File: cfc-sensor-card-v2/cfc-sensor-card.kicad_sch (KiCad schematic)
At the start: 6 parts

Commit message: Schematic Changes
Made schematic into hierarchy view. Revised OPD to match modern OPD. Removed connectors page. Separated power sequencing and PIRT sensor into 2 pages.
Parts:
- added J1: TFM-120-01-L-D-RA, oresat-connectors:J-SAMTEC-TFM-120-X1-XXX-D-RA, symbol oresat-connectors:J-SAMTEC-TFM-120-01-L-D-RA
- added J2: J-SAMTEC-TFM-110-X1-XXX-D-RA, oresat-connectors:J-SAMTEC-TFM-110-X1-XXX-D-RA, symbol oresat-connectors:J-SAMTEC-TFM-110-01-L-D-RA
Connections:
- new net C3-UART-RX: J1.38
- new net C3-UART-TX: J1.37
- new net CAN1_H: J1.33, J1.34
- new net CAN1_L: J1.35, J1.36
- new net CAN2_H: J1.17, J1.18
- new net CAN2_L: J1.19, J1.20
- new net GND: J1.27, J1.28, J1.29, J1.30
- new net OPD/OPD_PWR: J1.15, J1.16
- new net OPD/OPD_SCL: J1.13, J1.14
- new net OPD/OPD_SDA: J1.11, J1.12
- new net OUT1_N: J2.5, J2.6
- new net OUT1_P: J2.7, J2.8
- new net SENSOR_ENABLE: J2.13, J2.14
- new net SPI_CLK: J2.17, J2.18
- new net SPI_MISO: J2.15, J2.16
- new net SPI_MOSI: J2.19, J2.20
- new net TEC_ENABLE: J2.10, J2.9
- new net THERM+: J2.11, J2.12
- new net TXCLK_N: J2.1, J2.2
- new net TXCLK_P: J2.3, J2.4
- new net VBUS: J1.23, J1.24, J1.25, J1.26
- new net ~{SD}: J1.39, J1.40
- no-connect marks 0 -> 21
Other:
- sheet PIRT Sensor renamed Power Seqeuncing
- removed sheet Connectors
- added sheet PIRT (cfc-sensor-card-sch-PIRT.kicad_sch)
- sheet OPD ports: added OPD_PWR, OPD_SCL, OPD_SDA; removed none
- sheet Power Seqeuncing: file cfc-sensor-card-sch-pirt.kicad_sch -> cfc-sensor-card-sch-power.kicad_sch
- sheet Power Seqeuncing ports: added CLK_EN, SENSOR_ENABLE; removed none
- sheet TEC Control ports: added TEC+, TEC-, TEC_ENABLE; removed none
- note added: "Aux Connector"
- note added: "Future: route a "power is on" signal to the CFC Processor Card so it knows directly if the CFC Sensor Card is powered up or not."
- note added: "Main OreSat Card Connector (Backplane v2)"
- moved on the sheet: FID1, FID2, FID3, FID4, FID5, FID6

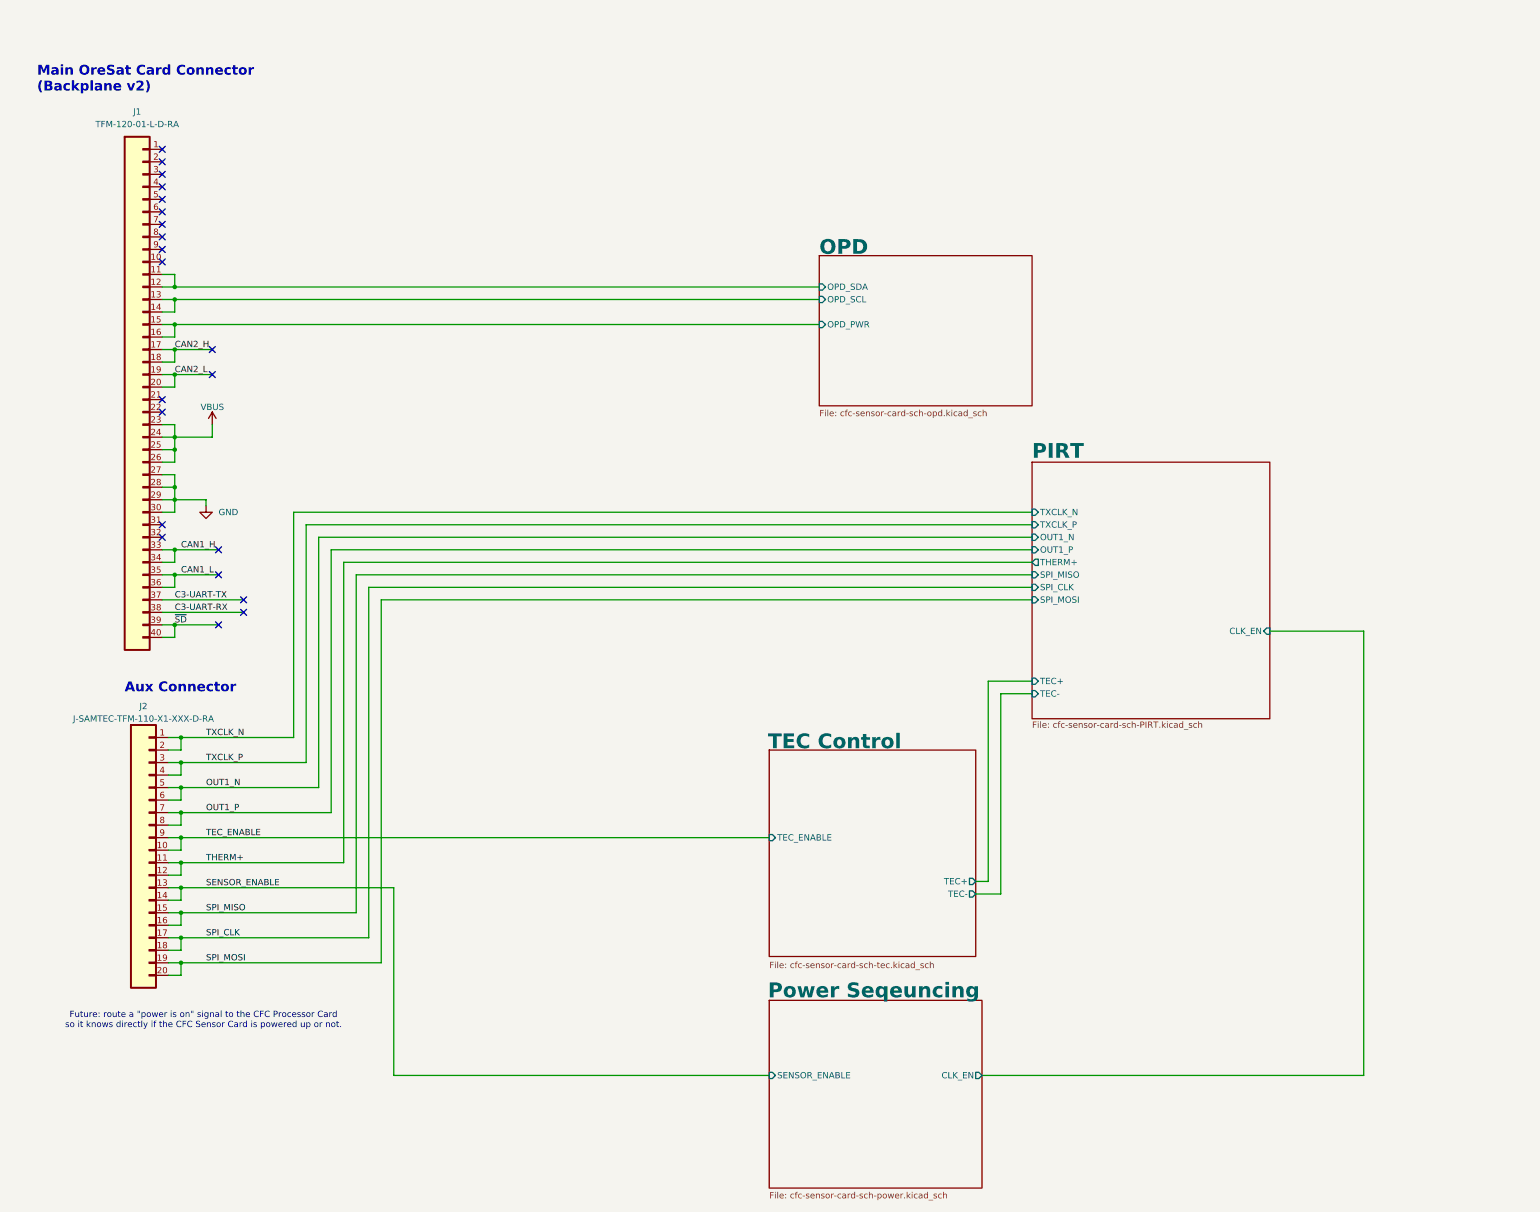
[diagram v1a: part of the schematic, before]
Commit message: Update
Fixed a couple of library issues on testpoints and other misc components. Added Pull up resistors to 8 channel i2c ic
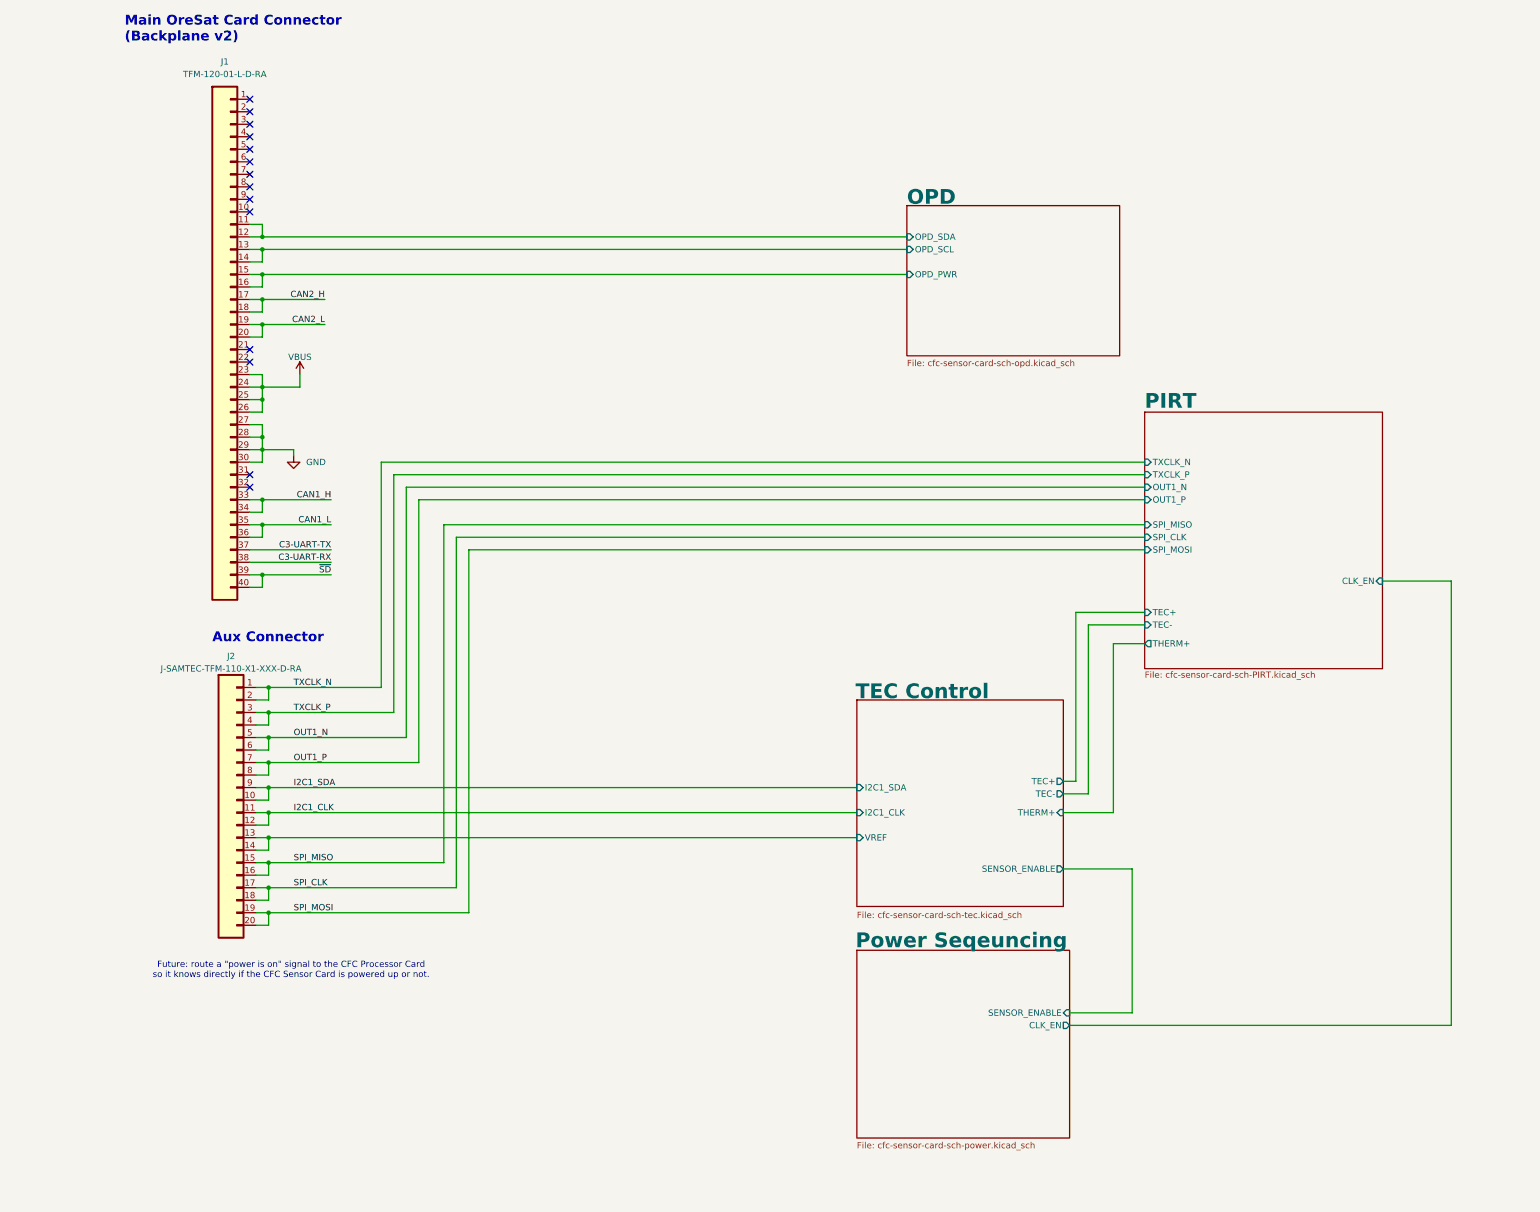
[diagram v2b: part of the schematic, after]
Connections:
- net SENSOR_ENABLE renamed TEC Control/VREF
- net TEC_ENABLE renamed I2C1_SDA
- net THERM+ renamed I2C1_CLK
- no-connect marks 21 -> 14
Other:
- sheet TEC Control ports: added I2C1_CLK, I2C1_SDA, SENSOR_ENABLE, THERM+, VREF; removed TEC_ENABLE
- moved on the sheet: J1, J2

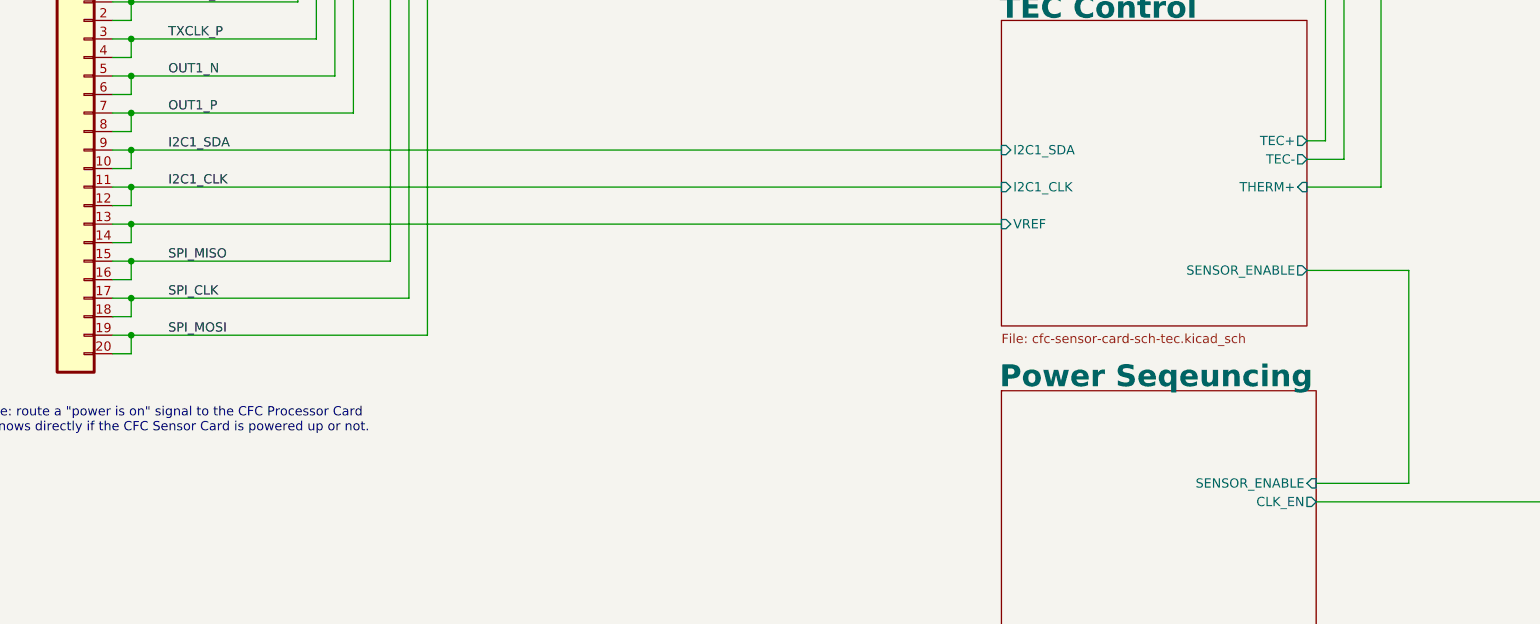
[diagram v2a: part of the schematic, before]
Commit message: Update
Added bidirectional TEC control with DRV8212 IC. Added Sensor enable pin back to processor; in case of i2c hang up octavo can still disable sensor.
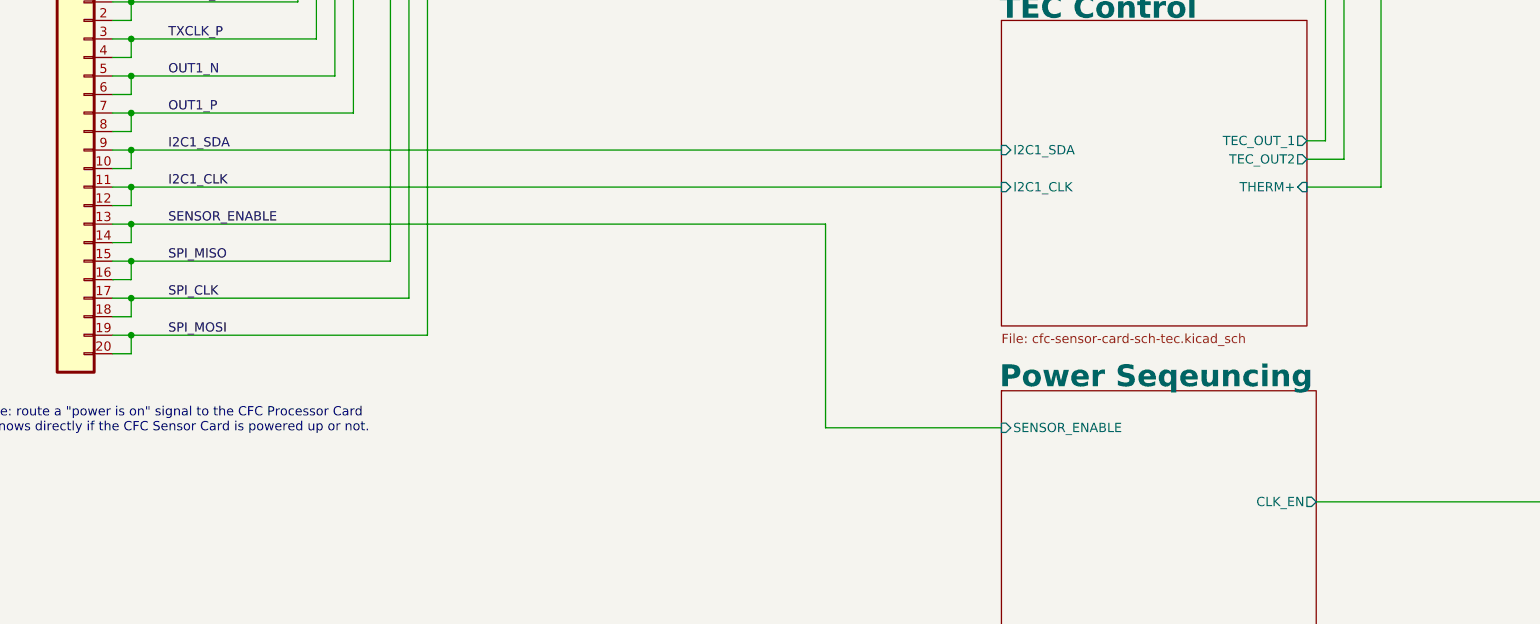
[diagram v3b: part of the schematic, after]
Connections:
- net TEC Control/VREF renamed SENSOR_ENABLE
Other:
- sheet TEC Control ports: added TEC_OUT2, TEC_OUT_1; removed SENSOR_ENABLE, TEC+, TEC-, VREF
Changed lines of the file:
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@@
+	)
+	(junction
+		(at 66.04 186.69)
+		(diameter 0)
+		(color 0 0 0 0)
 	)
 	(junction
@@
 	)
 	(junction
-		(at 66.04 186.69)
-		(diameter 0)
-		(color 0 0 0 0)
-	)
-	(junction
 		(at 64.77 107.95)
 		(diameter 0)
@@
 	(wire
 		(pts
+			(xy 66.04 186.69) (xy 161.29 186.69)
+		)
+		(stroke
+			(width 0)
+			(type default)
+		)
+	)
+	(wire
+		(pts
 			(xy 66.04 161.29) (xy 63.5 161.29)
 		)
@@
 	(wire
 		(pts
-			(xy 227.33 193.04) (xy 241.3 193.04)
-		)
-		(stroke
-			(width 0)
-			(type default)
-		)
-	)
-	(wire
-		(pts
 			(xy 66.04 201.93) (xy 63.5 201.93)
 		)
@@
 	(wire
 		(pts
-			(xy 66.04 186.69) (xy 185.42 186.69)
-		)
-		(stroke
-			(width 0)
-			(type default)
-		)
-	)
-	(wire
-		(pts
 			(xy 227.33 181.61) (xy 237.49 181.61)
 		)
@@
 	(wire
 		(pts
+			(xy 161.29 214.63) (xy 185.42 214.63)
+		)
+		(stroke
+			(width 0)
+			(type default)
+		)
+	)
+	(wire
+		(pts
 			(xy 228.6 224.79) (xy 306.07 224.79)
 		)
@@
 	(wire
 		(pts
-			(xy 241.3 222.25) (xy 228.6 222.25)
-		)
-		(stroke
-			(width 0)
-			(type default)
-		)
-	)
-	(wire
-		(pts
 			(xy 66.04 163.83) (xy 66.04 161.29)
 		)
@@
 	(wire
 		(pts
+			(xy 161.29 186.69) (xy 161.29 214.63)
+		)
+		(stroke
+			(width 0)
+			(type default)
+		)
+	)
+	(wire
+		(pts
 			(xy 64.77 123.19) (xy 78.74 123.19)
 		)
@@
 		(pts
 			(xy 63.5 171.45) (xy 66.04 171.45)
-		)
-		(stroke
-			(width 0)
-			(type default)
-		)
-	)
-	(wire
-		(pts
-			(xy 241.3 193.04) (xy 241.3 222.25)
 		)
 		(stroke
@@
 			)
 			(justify right bottom)
+		)
+	)
+	(label "SENSOR_ENABLE"
+		(at 71.12 186.69 0)
+		(effects
+			(font
+				(size 1.27 1.27)
+			)
+			(justify left bottom)
 		)
 	)
@@
 		)
 		(pin "SENSOR_ENABLE" input
-			(at 228.6 222.25 0)
-			(effects
-				(font
-					(size 1.27 1.27)
-				)
-				(justify right)
+			(at 185.42 214.63 180)
+			(effects
+				(font
+					(size 1.27 1.27)
+				)
+				(justify left)
 			)
 		)
@@
 			)
 		)
-		(pin "TEC-" output
-			(at 227.33 177.8 0)
-			(effects
-				(font
-					(size 1.27 1.27)
-				)
-				(justify right)
-			)
-		)
-		(pin "TEC+" output
-			(at 227.33 175.26 0)
-			(effects
-				(font
-					(size 1.27 1.27)
-				)
-				(justify right)
-			)
-		)
-		(pin "SENSOR_ENABLE" output
-			(at 227.33 193.04 0)
-			(effects
-				(font
-					(size 1.27 1.27)
-				)
-				(justify right)
-			)
-		)
-		(pin "VREF" input
-			(at 185.42 186.69 180)
-			(effects
-				(font
-					(size 1.27 1.27)
-				)
-				(justify left)
-			)
-		)
 		(pin "I2C1_SDA" input
 			(at 185.42 176.53 180)
@@
 			(effects
 				(font
+					(size 1.27 1.27)
+				)
+				(justify right)
+			)
+		)
+		(pin "TEC_OUT_1" output
+			(at 227.33 175.26 0)
+			(effects
+				(font
+					(size 1.27 1.27)
+				)
+				(justify right)
+			)
+		)
+		(pin "TEC_OUT2" output
+			(at 227.33 177.8 0)
+			(effects
+				(font

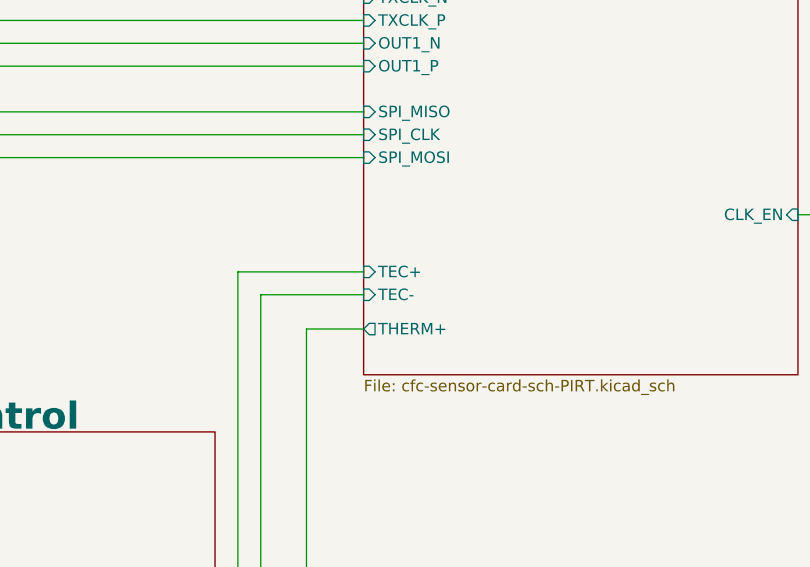
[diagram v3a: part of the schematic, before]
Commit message: update
Changed a couple of test points on OPD to through hole test points. Added tables to DRV8212 on sensor schematic+ other visual improvements to processor schematic.
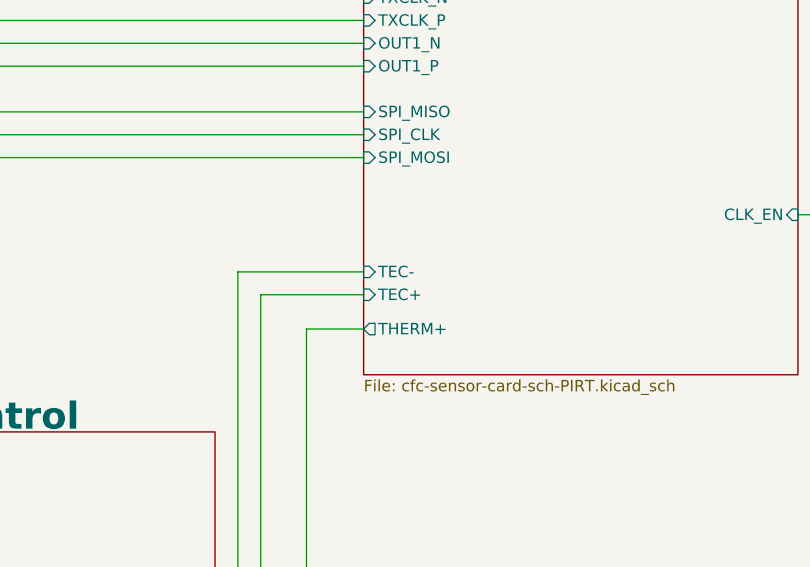
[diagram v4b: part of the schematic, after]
